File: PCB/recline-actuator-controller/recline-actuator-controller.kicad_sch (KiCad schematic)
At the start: 0 parts

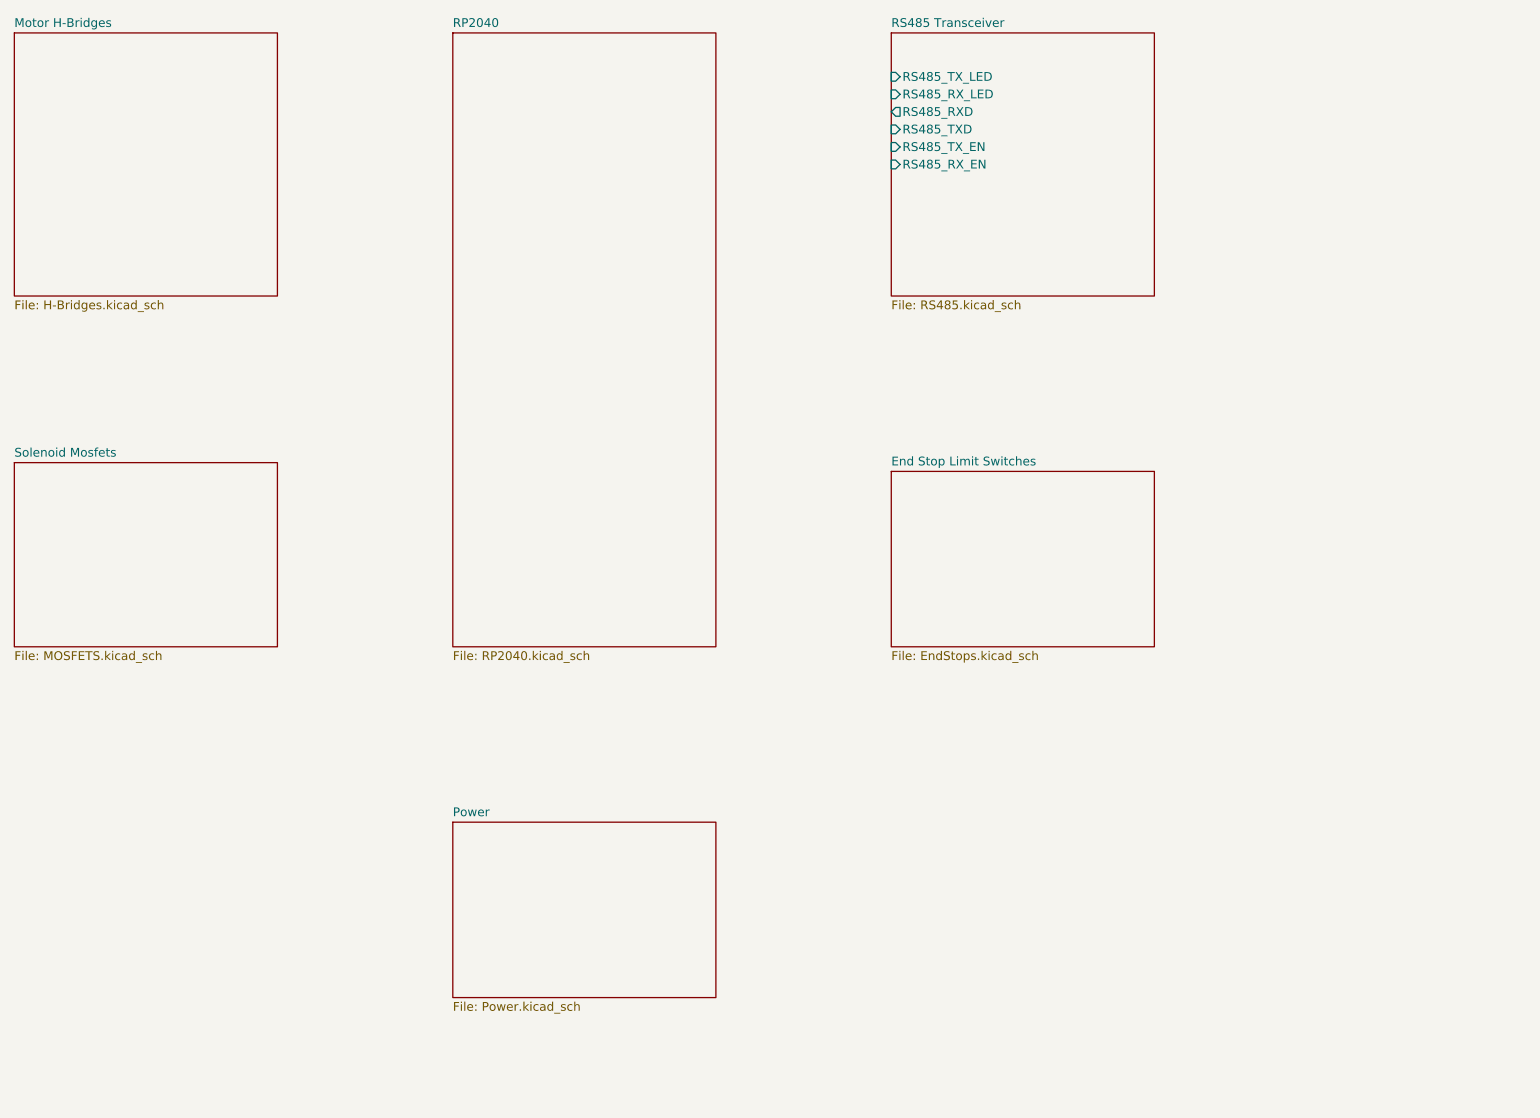
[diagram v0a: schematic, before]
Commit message: Recline Actuator Control
Recline controller board schematic and Recline actuator board schematics. Actuator control board schematic 90% complete.
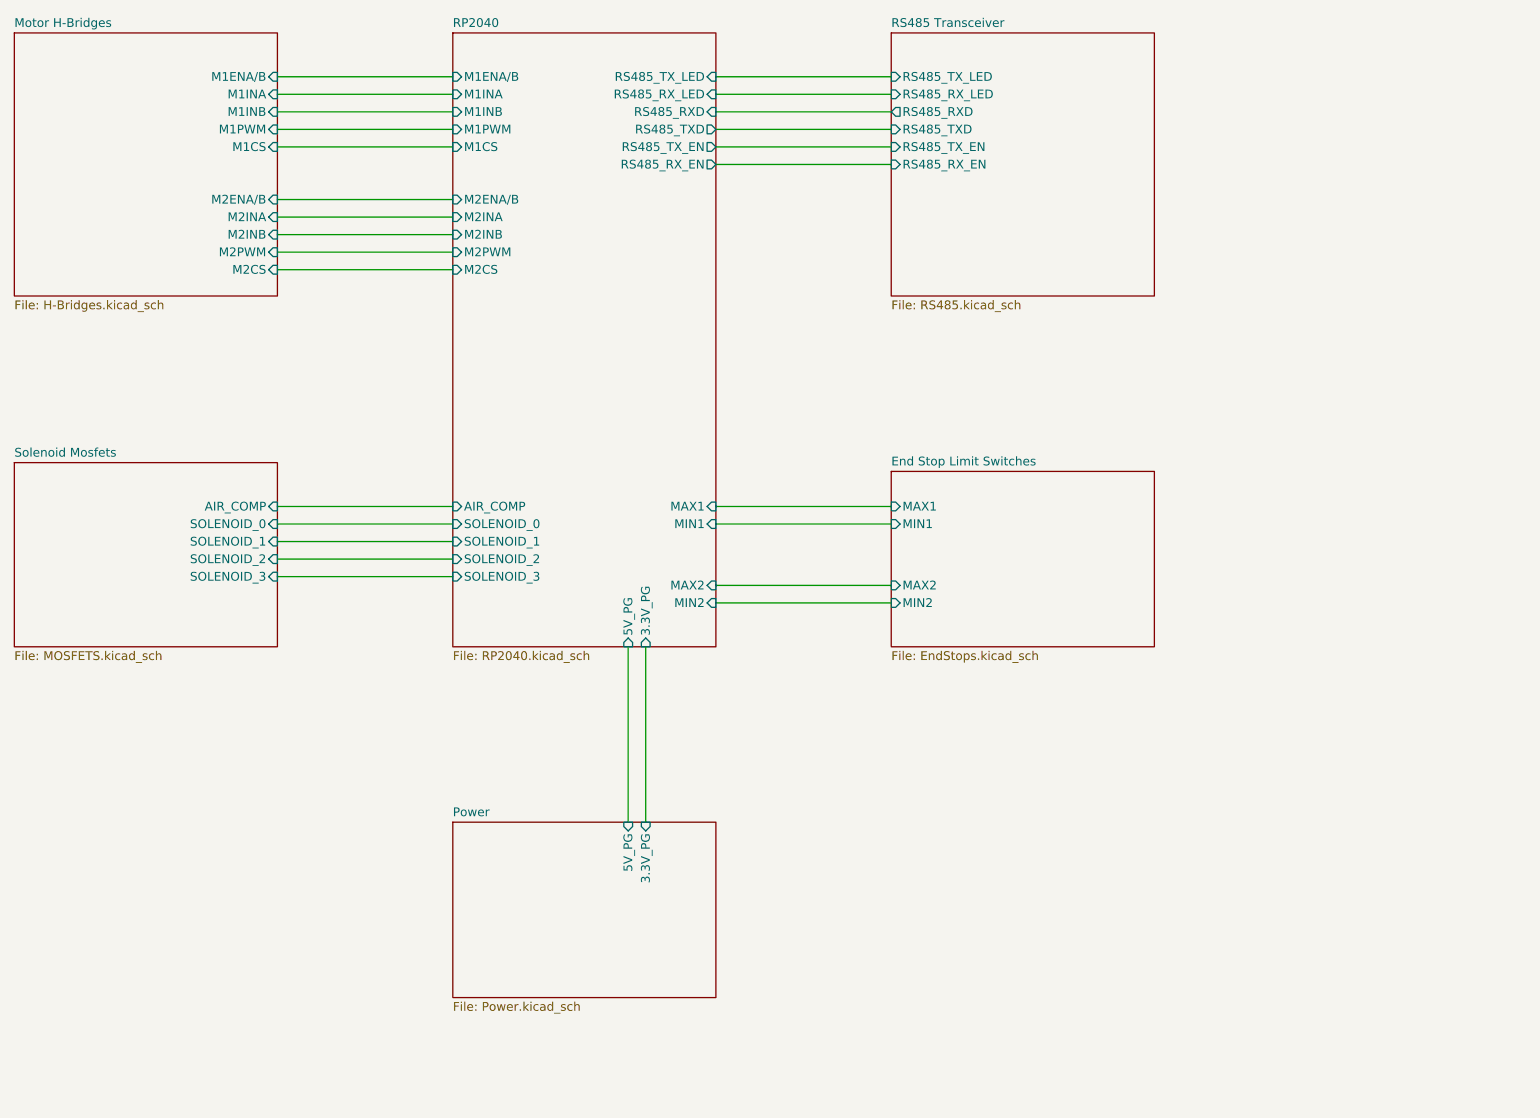
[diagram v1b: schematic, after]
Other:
- sheet End Stop Limit Switches ports: added MAX1, MAX2, MIN1, MIN2; removed none
- sheet Motor H-Bridges ports: added M1CS, M1ENA/B, M1INA, M1INB, M1PWM, M2CS, M2ENA/B, M2INA, M2INB, M2PWM; removed none
- sheet Power ports: added 3.3V_PG, 5V_PG; removed none
- sheet RP2040 ports: added 3.3V_PG, 5V_PG, AIR_COMP, M1CS, M1ENA/B, M1INA, M1INB, M1PWM, M2CS, M2ENA/B, M2INA, M2INB, M2PWM, MAX1, MAX2, MIN1, MIN2, RS485_RXD, RS485_RX_EN, RS485_RX_LED, RS485_TXD, RS485_TX_EN, RS485_TX_LED, SOLENOID_0, SOLENOID_1, SOLENOID_2, SOLENOID_3; removed none
- sheet Solenoid Mosfets ports: added AIR_COMP, SOLENOID_0, SOLENOID_1, SOLENOID_2, SOLENOID_3; removed none

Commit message: More Motor Channels
Adding more motor channels to actuator control board it will need new MCU or port expansion.
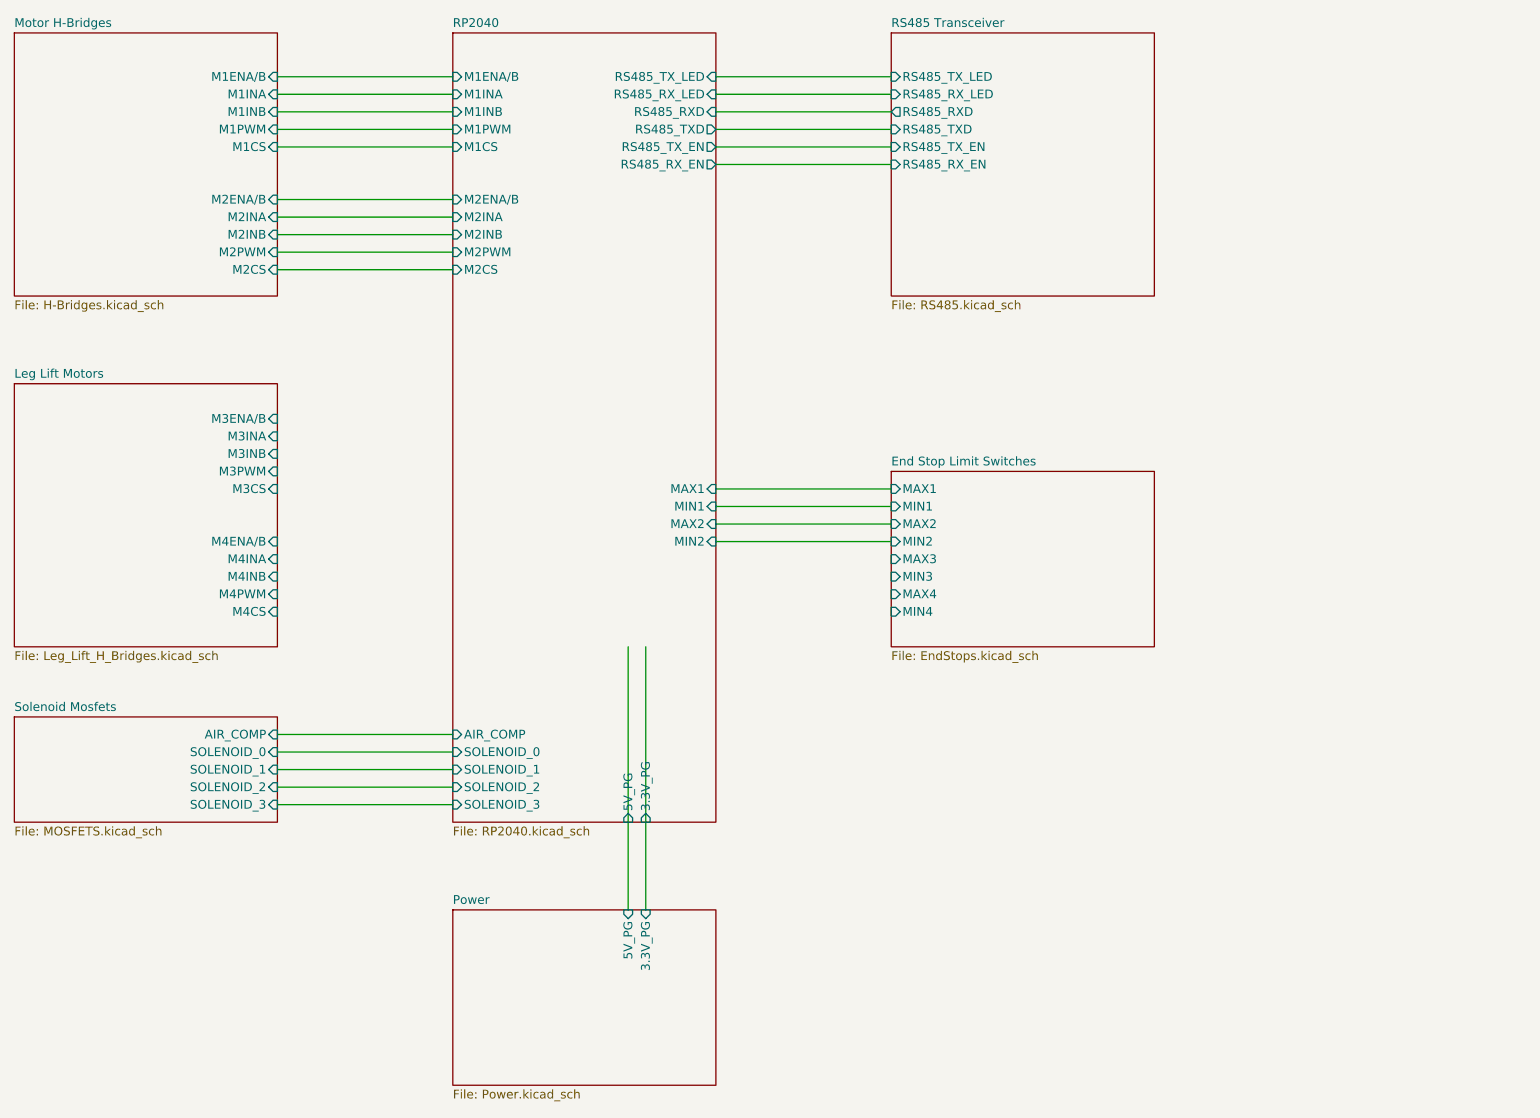
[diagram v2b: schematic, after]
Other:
- added sheet Leg Lift Motors (Leg_Lift_H_Bridges.kicad_sch)
- sheet End Stop Limit Switches ports: added MAX3, MAX4, MIN3, MIN4; removed none

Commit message: Recline Actuator Board Redesign
Recline actuator control board redesign complete, functionality extended to handle two additional large actuators for leg lifting. Air compressor switching circuit made to handle higher current. Additional end stops for additional actuators added, IO expander added for more input to RP2040. Current sensing for all 4 actuators.
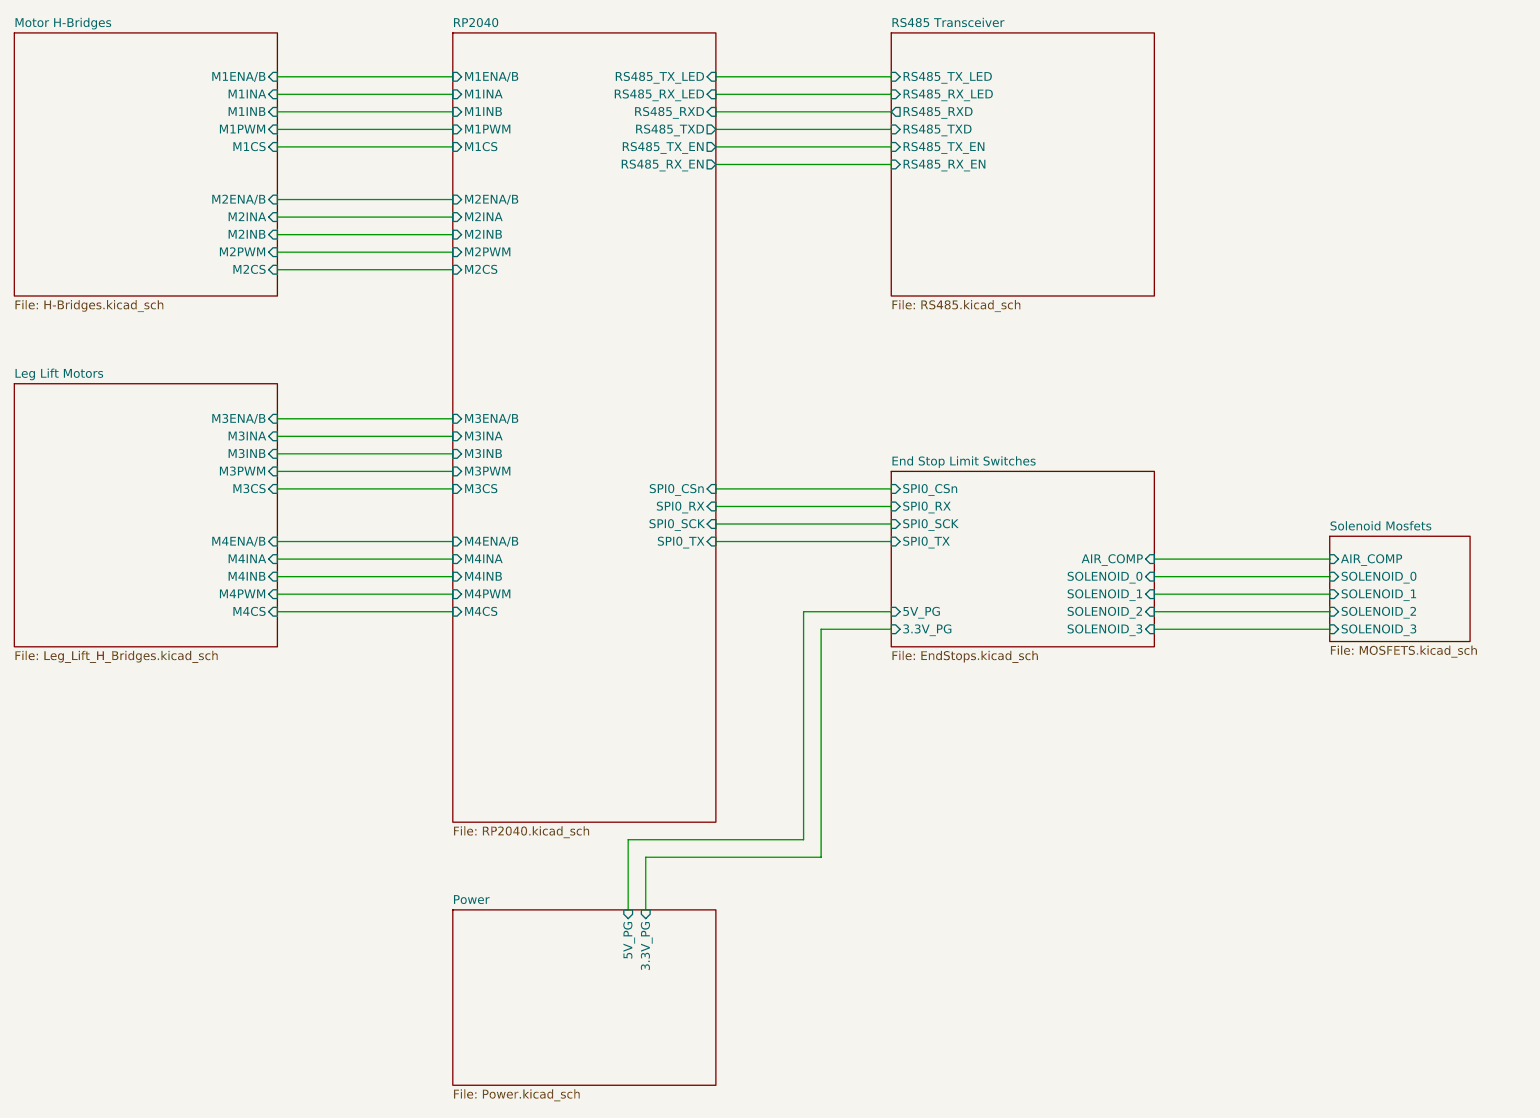
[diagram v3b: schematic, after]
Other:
- sheet End Stop Limit Switches ports: added 3.3V_PG, 5V_PG, AIR_COMP, SOLENOID_0, SOLENOID_1, SOLENOID_2, SOLENOID_3, SPI0_CSn, SPI0_RX, SPI0_SCK, SPI0_TX; removed MAX1, MAX2, MAX3, MAX4, MIN1, MIN2, MIN3, MIN4
- sheet RP2040 ports: added M3CS, M3ENA/B, M3INA, M3INB, M3PWM, M4CS, M4ENA/B, M4INA, M4INB, M4PWM, SPI0_CSn, SPI0_RX, SPI0_SCK, SPI0_TX; removed 3.3V_PG, 5V_PG, AIR_COMP, MAX1, MAX2, MIN1, MIN2, SOLENOID_0, SOLENOID_1, SOLENOID_2, SOLENOID_3

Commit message: Via Stichign and Pullups
Added optional pullups to endstop circuit.  Revised via stitching for input power, revised layout with added via stitching and copper pours for solenoid mosfets.
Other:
- sheet End Stop Limit Switches ports: added RS485_RX_LED2, RS485_TX_LED2; removed none
- sheet RS485 Transceiver ports: added RS485_RX_LED2, RS485_TX_LED2; removed none
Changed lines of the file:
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@@
+	(wire
+		(pts
+			(xy 241.3 106.68) (xy 241.3 71.12)
+		)
+		(stroke
+			(width 0)
+			(type default)
+		)
+	)
 	(wire
 		(pts
@@
 	(wire
 		(pts
+			(xy 238.76 73.66) (xy 238.76 104.14)
+		)
+		(stroke
+			(width 0)
+			(type default)
+		)
+	)
+	(wire
+		(pts
 			(xy 101.6 49.53) (xy 127 49.53)
 		)
@@
 	(wire
 		(pts
+			(xy 228.6 73.66) (xy 238.76 73.66)
+		)
+		(stroke
+			(width 0)
+			(type default)
+		)
+	)
+	(wire
+		(pts
 			(xy 228.6 124.46) (xy 254 124.46)
 		)
@@
 	(wire
 		(pts
+			(xy 228.6 106.68) (xy 241.3 106.68)
+		)
+		(stroke
+			(width 0)
+			(type default)
+		)
+	)
+	(wire
+		(pts
 			(xy 165.1 109.22) (xy 190.5 109.22)
 		)
@@
 	(wire
 		(pts
+			(xy 228.6 104.14) (xy 238.76 104.14)
+		)
+		(stroke
+			(width 0)
+			(type default)
+		)
+	)
+	(wire
+		(pts
 			(xy 101.6 114.3) (xy 127 114.3)
 		)
@@
 		(pts
 			(xy 165.1 44.45) (xy 190.5 44.45)
+		)
+		(stroke
+			(width 0)
+			(type default)
+		)
+	)
+	(wire
+		(pts
+			(xy 241.3 71.12) (xy 228.6 71.12)
 		)
 		(stroke
@@
 			)
 		)
+		(pin "RS485_TX_LED2" input
+			(at 228.6 106.68 0)
+			(effects
+				(font
+					(size 1.27 1.27)
+				)
+				(justify right)
+			)
+		)
+		(pin "RS485_RX_LED2" input
+			(at 228.6 104.14 0)
+			(effects
+				(font
+					(size 1.27 1.27)
+				)
+				(justify right)
+			)
+		)
 		(instances
 			(project "recline-actuator-controller"
@@
 			)
 		)
+		(pin "RS485_RX_LED2" input
+			(at 228.6 73.66 0)
+			(effects
+				(font
+					(size 1.27 1.27)
+				)
+				(justify right)
+			)
+		)
+		(pin "RS485_TX_LED2" input
+			(at 228.6 71.12 0)
+			(effects
+				(font
+					(size 1.27 1.27)
+				)
+				(justify right)
+			)
+		)
